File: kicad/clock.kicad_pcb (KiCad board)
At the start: 4 copper layers, 87 x 38 mm, 56 parts, among them P1 CONN_01X03, SW1 SWITCH_MIN, SW2 SWITCH_HR, U1 74LS90, U10 74LS247, U11 74LS73, U2 74LS90, U3 MAX6817, U4 74LS90, U5 74LS247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

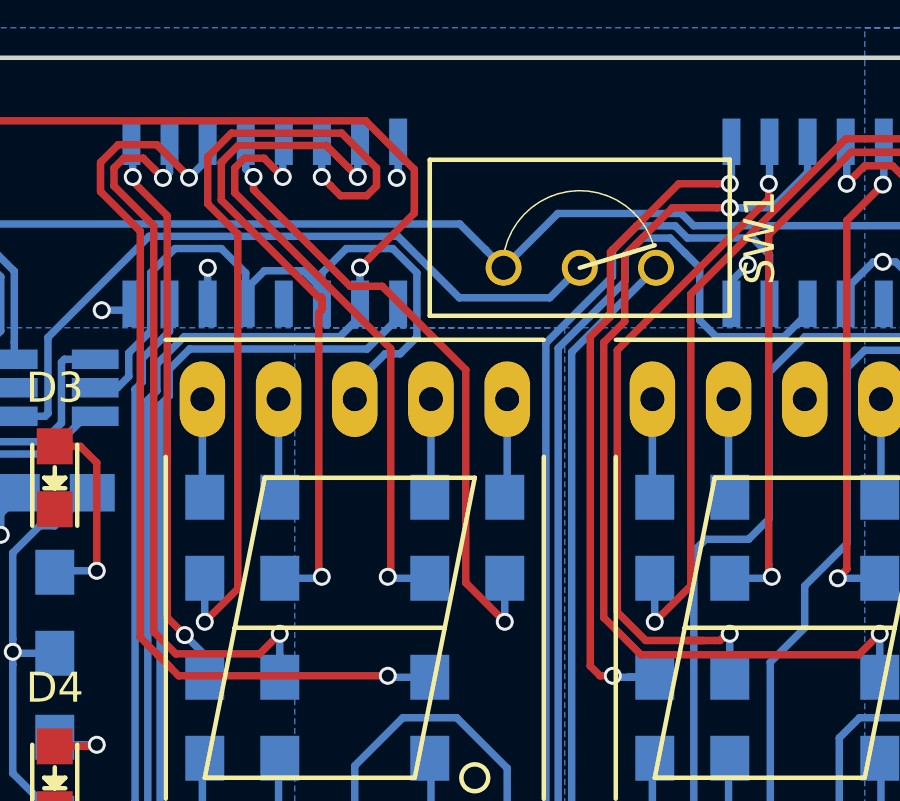
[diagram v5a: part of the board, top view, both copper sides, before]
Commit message: Scooch a few tracks
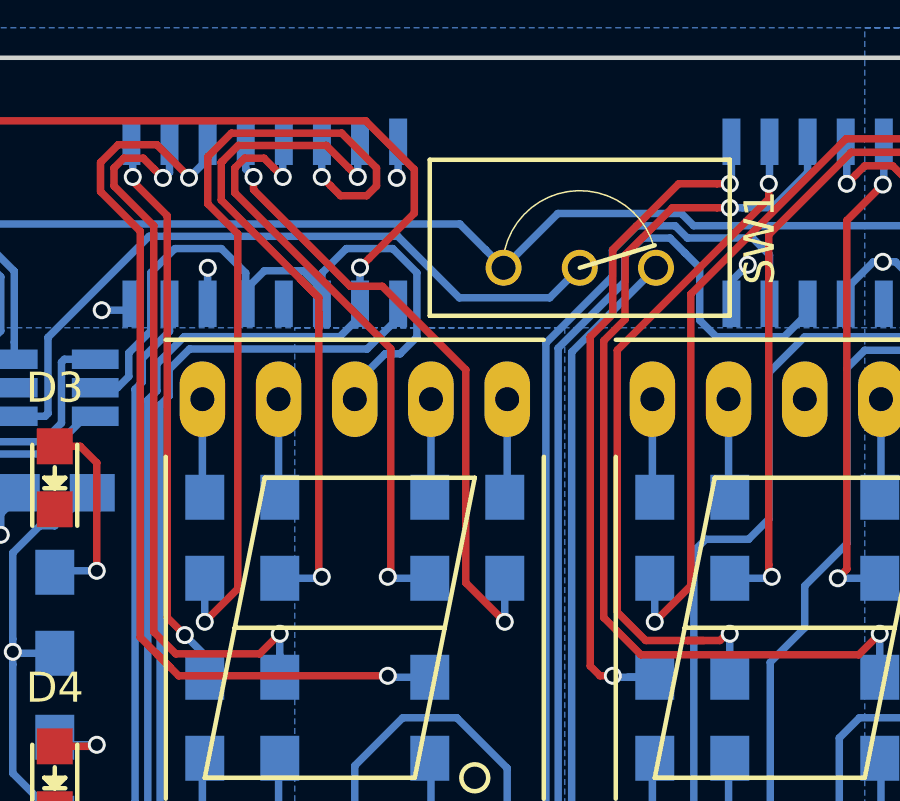
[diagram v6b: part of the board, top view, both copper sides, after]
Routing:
- net /min_ten_f: track 23.6 -> 24.4 mm
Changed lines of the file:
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@@
-(kicad_pcb (version 4) (host pcbnew 4.0.4-1.fc25-product)
+(kicad_pcb (version 4) (host pcbnew 4.0.5)
   (general
     (links 180)
@@
   (segment (start 159.92 103.62) (end 159.92 100.43) (width 0.25) (layer B.Cu) (net 34) (status 30))
   (segment (start 159.92 100.43) (end 160 100.35) (width 0.25) (layer B.Cu) (net 34) (status 30))
+  (segment (start 163.801291 86) (end 163.801291 85.498709) (width 0.25) (layer F.Cu) (net 35))
+  (segment (start 163.801291 94.201291) (end 163.801291 86) (width 0.25) (layer F.Cu) (net 35))
+  (segment (start 163.801291 84.992559) (end 163.2 84.391268) (width 0.25) (layer F.Cu) (net 35))
+  (segment (start 163.786859 84.978127) (end 163.2 84.391268) (width 0.25) (layer F.Cu) (net 35))
+  (segment (start 163.801291 86) (end 163.801291 84.992559) (width 0.25) (layer F.Cu) (net 35))
+  (segment (start 163.2 84.391268) (end 160.550012 81.74128) (width 0.25) (layer F.Cu) (net 35))
   (segment (start 163.9 94.3) (end 163.801291 94.201291) (width 0.25) (layer F.Cu) (net 35))
-  (segment (start 163.801291 94.201291) (end 163.801291 85.498709) (width 0.25) (layer F.Cu) (net 35))
-  (segment (start 163.801291 85.498709) (end 163.9 85.4) (width 0.25) (layer F.Cu) (net 35))
   (segment (start 160.550013 80.486907) (end 160.6 80.43692) (width 0.25) (layer F.Cu) (net 35))
   (segment (start 160.6 80.43692) (end 161.114251 79.922669) (width 0.25) (layer F.Cu) (net 35))
   (segment (start 160.550012 81.74128) (end 160.550012 80.486908) (width 0.25) (layer F.Cu) (net 35))
   (segment (start 160.550012 80.486908) (end 160.6 80.43692) (width 0.25) (layer F.Cu) (net 35))
-  (segment (start 163.9 84.978127) (end 163.786859 84.978127) (width 0.25) (layer F.Cu) (net 35))
-  (segment (start 163.786859 84.978127) (end 160.550012 81.74128) (width 0.25) (layer F.Cu) (net 35))
-  (segment (start 163.9 85.4) (end 163.9 85.034698) (width 0.25) (layer F.Cu) (net 35))
-  (segment (start 163.9 85.4) (end 163.9 84.978127) (width 0.25) (layer F.Cu) (net 35))
   (segment (start 162.5 94.35) (end 163.85 94.35) (width 0.25) (layer B.Cu) (net 35))
   (via (at 163.9 94.3) (size 0.6) (drill 0.4) (layers F.Cu B.Cu) (net 35))
@@
   (segment (start 185.08 88.38) (end 185.08 91.57) (width 0.25) (layer B.Cu) (net 42) (status 30))
   (segment (start 185.08 91.57) (end 185 91.65) (width 0.25) (layer B.Cu) (net 42) (status 30))
+  (segment (start 173.299838 86.430897) (end 174.008966 85.721769) (width 0.25) (layer F.Cu) (net 43))
   (segment (start 177.076413 81.999217) (end 177.500677 81.999217) (width 0.25) (layer F.Cu) (net 43))
-  (segment (start 173.999437 83.587444) (end 175.587664 81.999217) (width 0.25) (layer F.Cu) (net 43))
-  (segment (start 173.299838 86.487465) (end 173.999437 85.787867) (width 0.25) (layer F.Cu) (net 43))
-  (segment (start 173.999437 85.787867) (end 173.999437 83.587444) (width 0.25) (layer F.Cu) (net 43))
+  (segment (start 175.587664 81.999217) (end 177.076413 81.999217) (width 0.25) (layer F.Cu) (net 43))
+  (segment (start 174.008966 85.721769) (end 174.008966 83.577915) (width 0.25) (layer F.Cu) (net 43))
+  (segment (start 173.299838 95.661251) (end 173.299838 86.430897) (width 0.25) (layer F.Cu) (net 43))
+  (segment (start 181.799753 96.900247) (end 174.538834 96.900247) (width 0.25) (layer F.Cu) (net 43))
+  (segment (start 182.5 96.2) (end 181.799753 96.900247) (width 0.25) (layer F.Cu) (net 43))
+  (segment (start 174.008966 83.577915) (end 175.587664 81.999217) (width 0.25) (layer F.Cu) (net 43))
   (segment (start 174.538834 96.900247) (end 173.299838 95.661251) (width 0.25) (layer F.Cu) (net 43))
-  (segment (start 181.799753 96.900247) (end 174.538834 96.900247) (width 0.25) (layer F.Cu) (net 43))
-  (segment (start 173.299838 95.661251) (end 173.299838 86.487465) (width 0.25) (layer F.Cu) (net 43))
-  (segment (start 175.587664 81.999217) (end 177.076413 81.999217) (width 0.25) (layer F.Cu) (net 43))
-  (segment (start 182.5 96.2) (end 181.799753 96.900247) (width 0.25) (layer F.Cu) (net 43))
   (segment (start 177.924941 81.999217) (end 177.500677 81.999217) (width 0.25) (layer B.Cu) (net 43))
   (segment (start 178.920783 81.999217) (end 177.924941 81.999217) (width 0.25) (layer B.Cu) (net 43))
@@
   (segment (start 177.46 103.62) (end 177.46 100.39) (width 0.25) (layer B.Cu) (net 46) (status 30))
   (segment (start 177.46 100.39) (end 177.5 100.35) (width 0.25) (layer B.Cu) (net 46) (status 30))
+  (segment (start 172.849828 97.274092) (end 172.849828 86.301064) (width 0.25) (layer F.Cu) (net 47))
+  (segment (start 173.598955 83.398919) (end 175.798669 81.199205) (width 0.25) (layer F.Cu) (net 47))
+  (segment (start 175.798669 81.199205) (end 177.075934 81.199205) (width 0.25) (layer F.Cu) (net 47))
+  (segment (start 173.598955 85.551937) (end 173.598955 83.398919) (width 0.25) (layer F.Cu) (net 47))
+  (segment (start 173.6 97.6) (end 173.175736 97.6) (width 0.25) (layer F.Cu) (net 47))
+  (segment (start 173.175736 97.6) (end 172.849828 97.274092) (width 0.25) (layer F.Cu) (net 47))
+  (segment (start 172.849828 86.301064) (end 173.598955 85.551937) (width 0.25) (layer F.Cu) (net 47))
   (segment (start 177.075934 81.199205) (end 177.500198 81.199205) (width 0.25) (layer F.Cu) (net 47))
-  (segment (start 175.798669 81.199205) (end 177.075934 81.199205) (width 0.25) (layer F.Cu) (net 47))
-  (segment (start 173.524073 83.473801) (end 175.798669 81.199205) (width 0.25) (layer F.Cu) (net 47))
-  (segment (start 173.524073 85.62682) (end 173.524073 83.473801) (width 0.25) (layer F.Cu) (net 47))
-  (segment (start 172.849828 86.301064) (end 173.524073 85.62682) (width 0.25) (layer F.Cu) (net 47))
-  (segment (start 172.849828 97.274092) (end 172.849828 86.301064) (width 0.25) (layer F.Cu) (net 47))
-  (segment (start 173.175736 97.6) (end 172.849828 97.274092) (width 0.25) (layer F.Cu) (net 47))
-  (segment (start 173.6 97.6) (end 173.175736 97.6) (width 0.25) (layer F.Cu) (net 47))
   (segment (start 175 97.65) (end 173.65 97.65) (width 0.25) (layer B.Cu) (net 47))
   (segment (start 173.65 97.65) (end 173.6 97.6) (width 0.25) (layer B.Cu) (net 47))

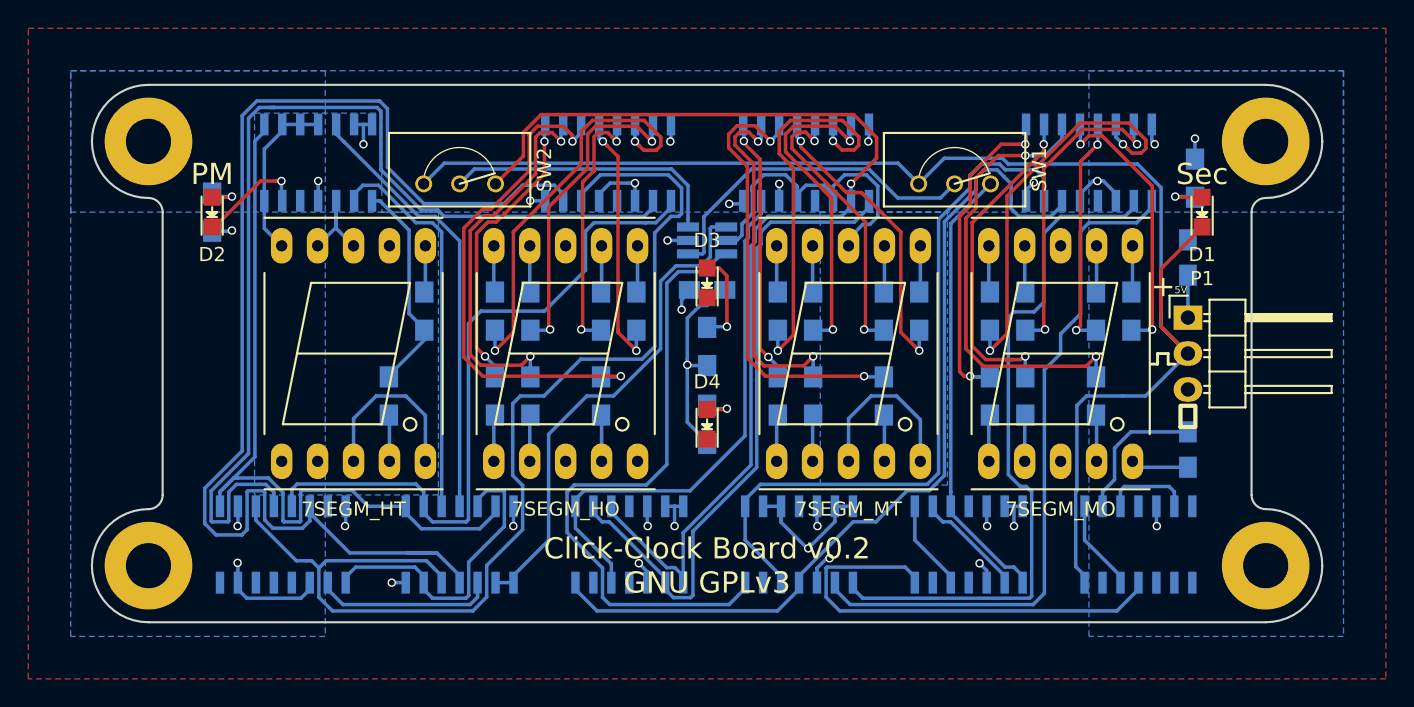
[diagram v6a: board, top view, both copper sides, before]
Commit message: Set the mounting hole pitch to be 80mm x 30mm
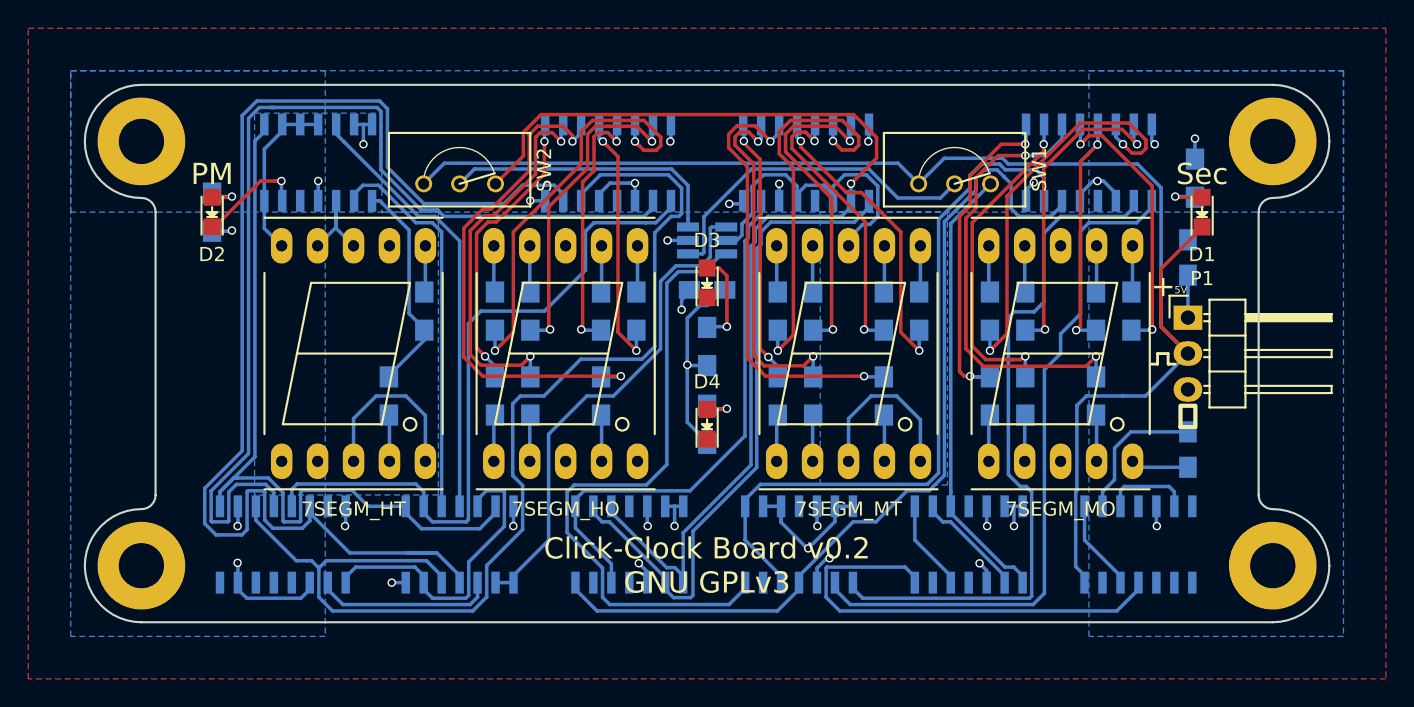
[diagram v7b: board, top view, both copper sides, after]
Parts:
- moved REF** 0.50 mm to (195.0, 111.0)
- moved REF** 0.50 mm to (115.0, 111.0)
- moved REF** 0.50 mm to (115.0, 81.0)
- moved REF** 0.50 mm to (195.0, 81.0)
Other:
- board size 87 x 38 mm -> 88 x 38 mm
